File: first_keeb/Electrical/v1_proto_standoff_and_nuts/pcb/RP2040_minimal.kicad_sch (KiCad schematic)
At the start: 63 parts, among them J1 Conn_01x04_Socket, P1 USB-TYPE-C-016, Q1 BSS138, SW3 TS-1187A-B-A-B, SW5 TS-1187A-B-A-B, SW6 BUTT1, SW7 BUTT3, SW8 BUTT2, U1 ME6208A44M3G, U2 ME6212C25M5G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

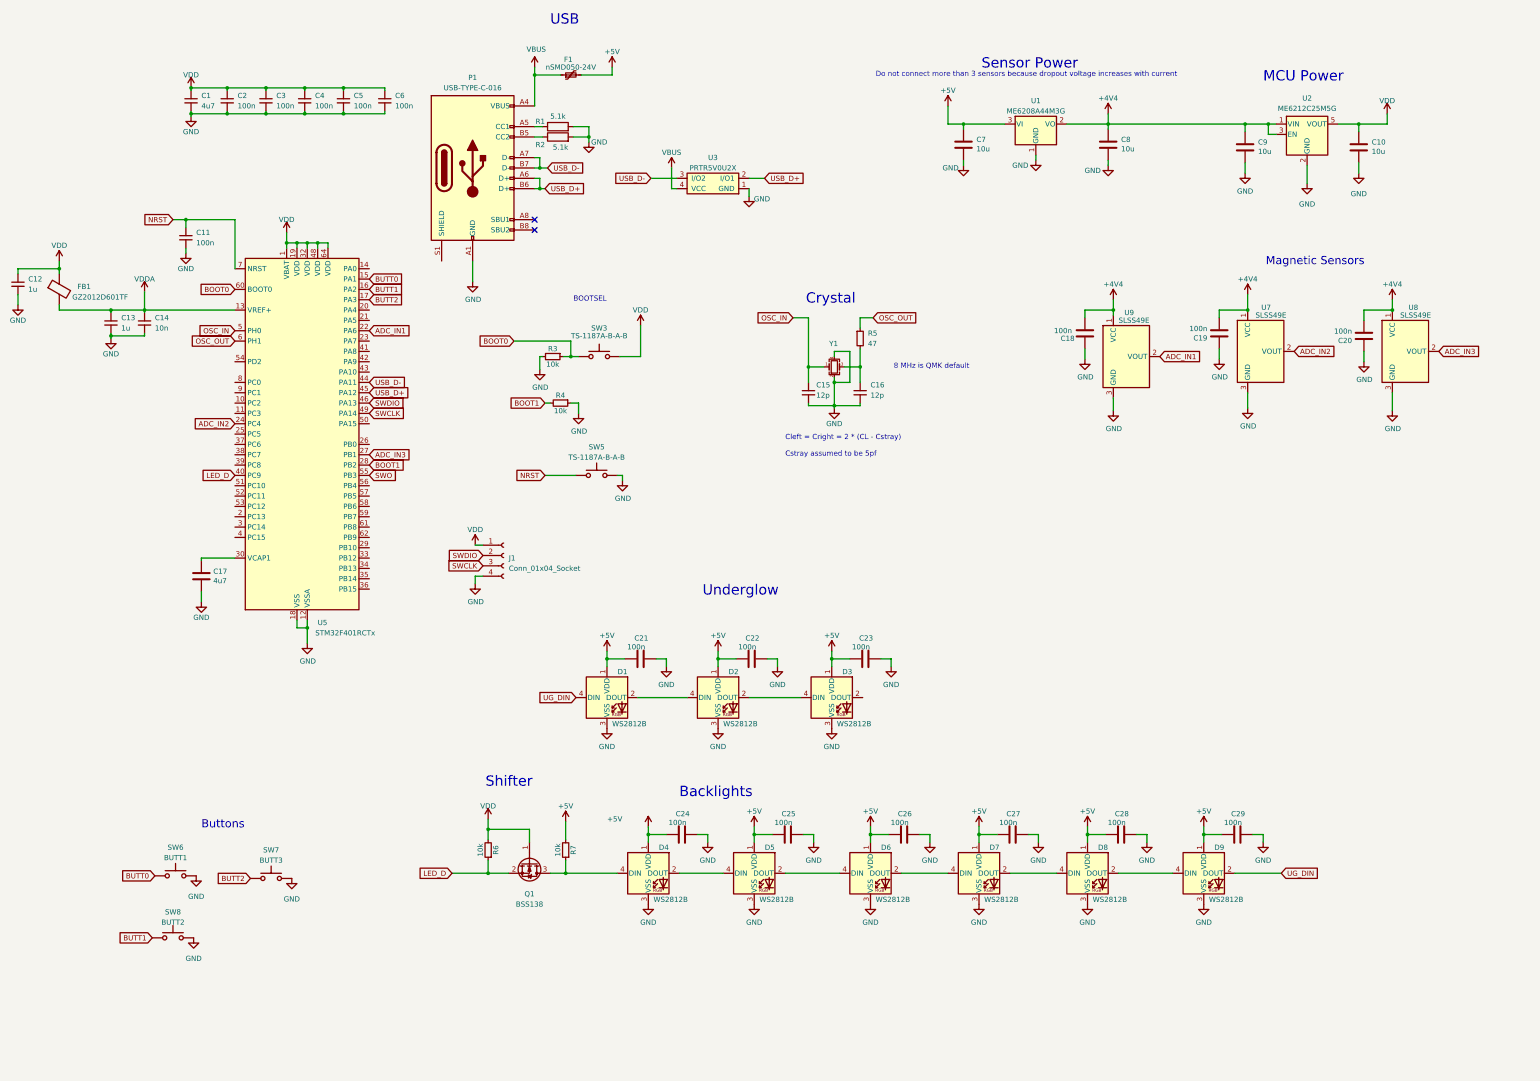
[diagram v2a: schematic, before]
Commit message: finishes stm with 3d printed standoff holes
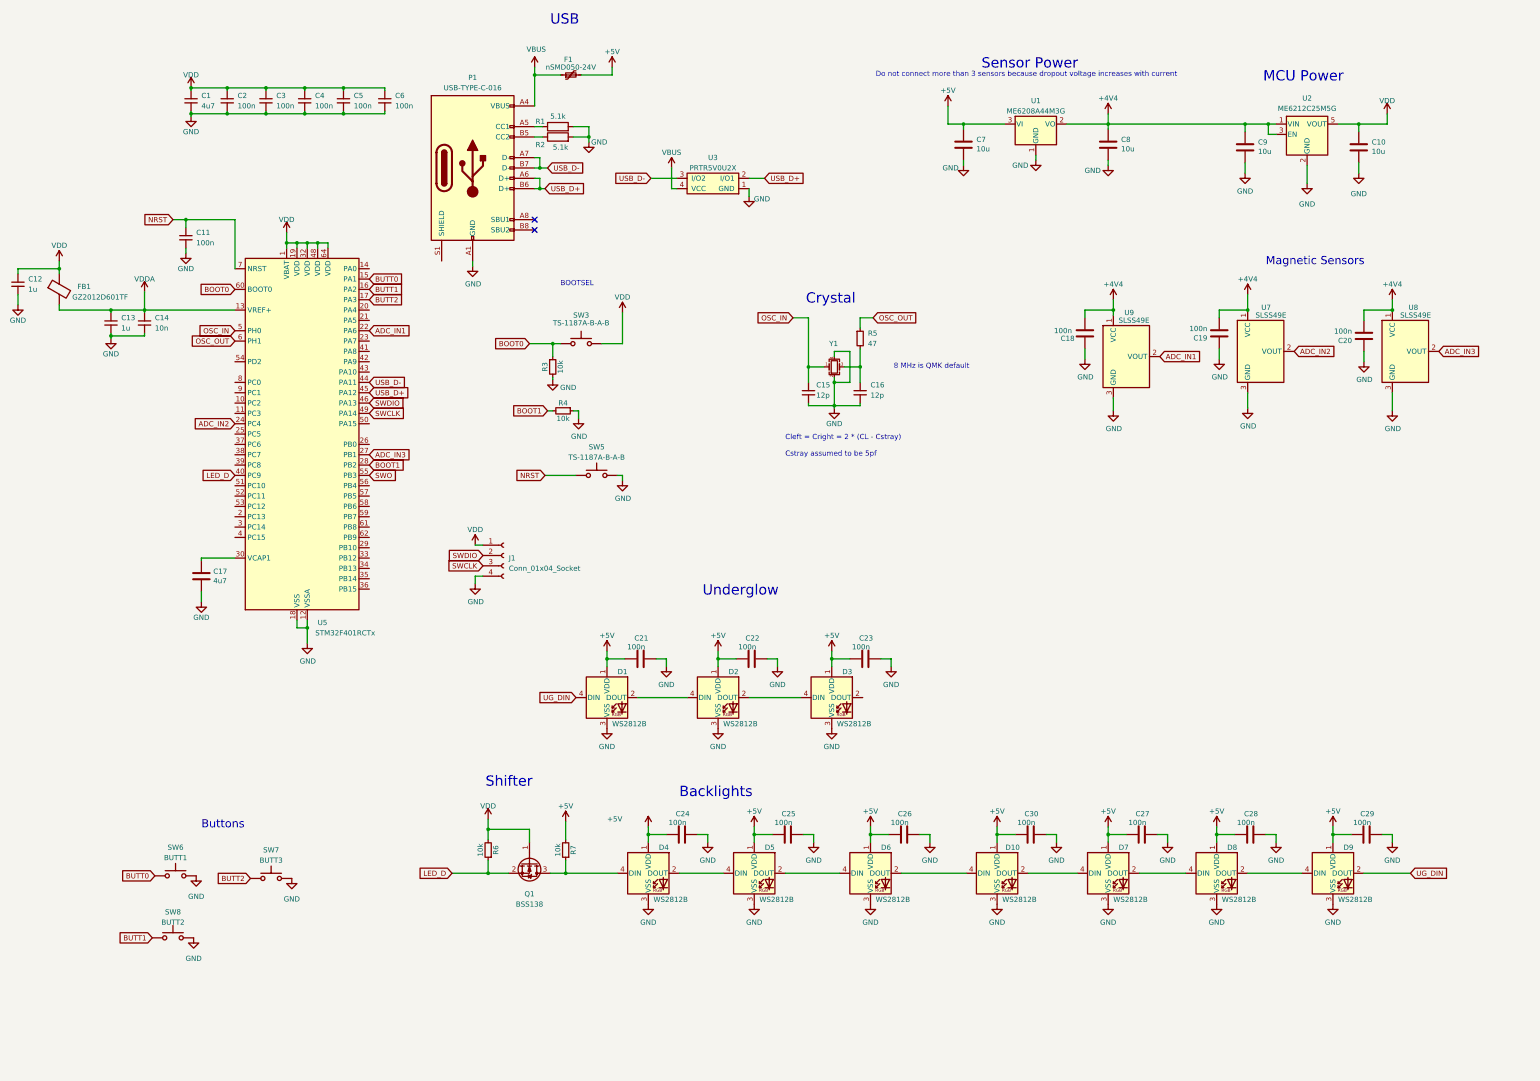
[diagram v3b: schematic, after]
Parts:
- added C30: 100n, Capacitor_SMD:C_0402_1005Metric, symbol Device:C
- added D10: WS2812B, LED_SMD:LED_WS2812B_PLCC4_5.0x5.0mm_P3.2mm, symbol LED:WS2812B
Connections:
- net +5V: now also C30.1, D10.1 (VDD)
- net GND: now also C30.2, D10.3 (VSS)
- net at D7.4 (DIN): now also D10.2 (DOUT); no longer D6.2 (DOUT)
- new net: D10.4 (DIN), D6.2 (DOUT)
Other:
- moved on the sheet: C27, C28, C29, D7, D8, D9, R3, R4, SW3
